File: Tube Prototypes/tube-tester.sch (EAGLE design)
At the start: 33 parts, among them IC1 NE555D, IC2 74141N, IC3 7805, Q1 IRF740S, Q2 BC546

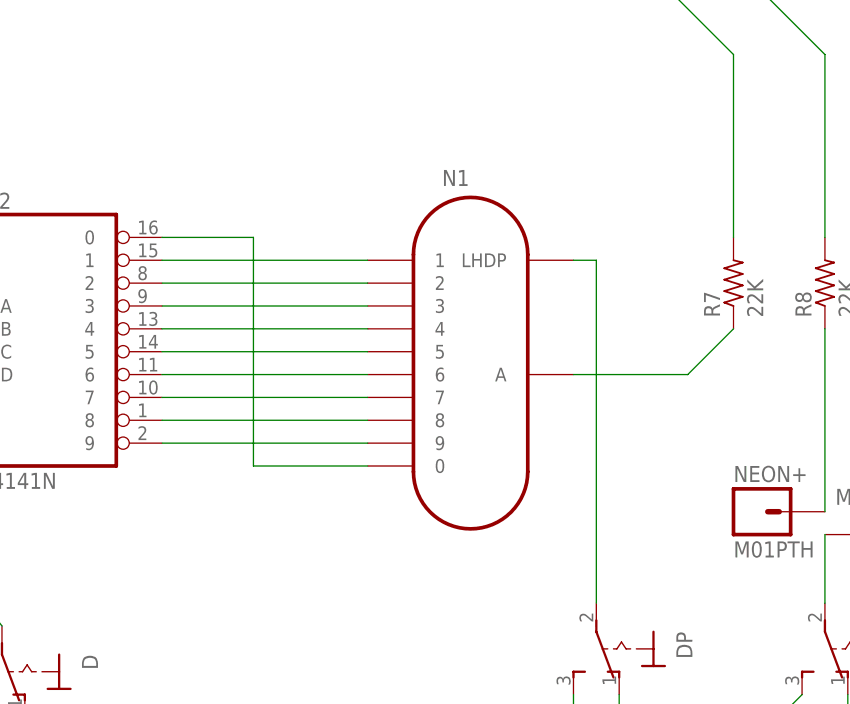
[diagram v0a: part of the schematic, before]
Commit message: new 180V and tube tester
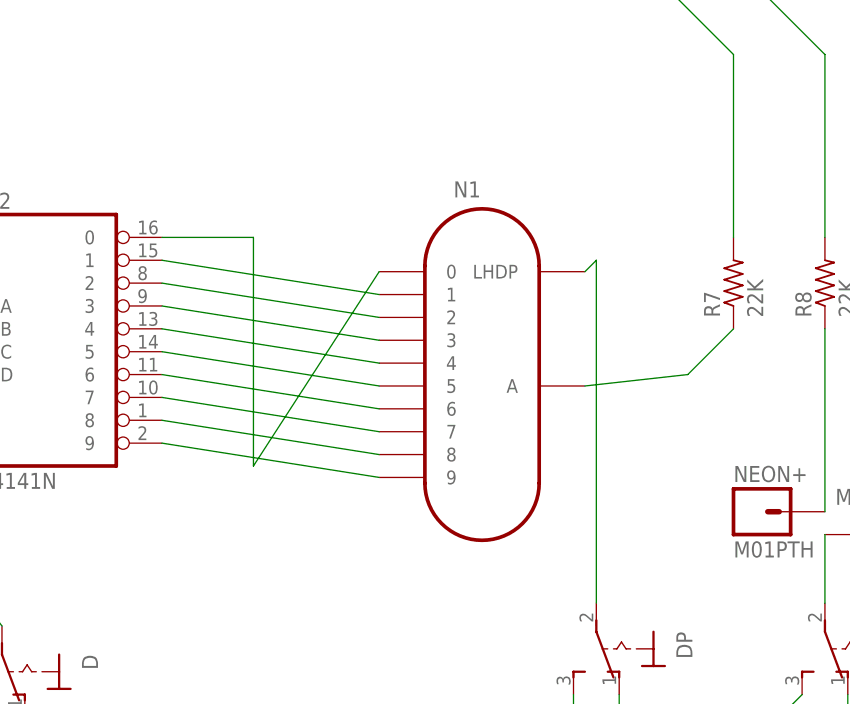
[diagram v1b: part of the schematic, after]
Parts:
- N1: value IN-12BIN-12 -> IN-12B; device iStivi - Tubes:IN-12BIN-12 -> iStivi - Tubes:IN-12B
- Q2: device iStivi - Transistor-FET:BC546B -> iStivi - Transistor-FET-reg:BC546A
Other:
- moved on the sheet: N1
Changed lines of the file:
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@@
 <part name="R6" library="iStivi - RCLD" deviceset="RESISTOR" device="R1206" value="2K2"/>
 <part name="C3" library="iStivi - RCLD" deviceset="CAPACITOR" device="C1206K" value="100pF"/>
-<part name="Q2" library="iStivi - Transistor-FET" deviceset="BC546*" device="" technology="B" value="BC546"/>
+<part name="Q2" library="iStivi - Transistor-FET-reg" deviceset="BC546*" device="" technology="A" value="BC546"/>
 <part name="C2" library="iStivi - RCLD" deviceset="CAPACITOR" device="C1206K" value="2n2"/>
 <part name="L1" library="iStivi - RCLD" deviceset="INDUCTOR" device="0207/10" value="100uH"/>
@@
 <part name="GND1" library="iStivi - Supply" deviceset="GND" device=""/>
 <part name="IC2" library="iStivi - ICs" deviceset="74*141" device="N"/>
-<part name="N1" library="iStivi - Tubes" deviceset="IN-12B" device="IN-12"/>
+<part name="N1" library="iStivi - Tubes" deviceset="IN-12B" device=""/>
 <part name="R7" library="iStivi - RCLD" deviceset="RESISTOR" device="0207/10" value="22K"/>
 <part name="A" library="iStivi - Button-Switch" deviceset="320-916" device=""/>
@@
 <pinref part="N1" gate="G$1" pin="1"/>
 <pinref part="IC2" gate="A" pin="1"/>
-<wire x1="213.36" y1="73.66" x2="190.5" y2="73.66" width="0.1524" layer="91"/>
+<wire x1="214.63" y1="69.85" x2="190.5" y2="73.66" width="0.1524" layer="91"/>
 </segment>
 </net>
@@
 <pinref part="N1" gate="G$1" pin="2"/>
 <pinref part="IC2" gate="A" pin="2"/>
-<wire x1="213.36" y1="71.12" x2="190.5" y2="71.12" width="0.1524" layer="91"/>
+<wire x1="214.63" y1="67.31" x2="190.5" y2="71.12" width="0.1524" layer="91"/>
 </segment>
 </net>
@@
 <pinref part="N1" gate="G$1" pin="3"/>
 <pinref part="IC2" gate="A" pin="3"/>
-<wire x1="213.36" y1="68.58" x2="190.5" y2="68.58" width="0.1524" layer="91"/>
+<wire x1="214.63" y1="64.77" x2="190.5" y2="68.58" width="0.1524" layer="91"/>
 </segment>
 </net>
@@
 <pinref part="N1" gate="G$1" pin="4"/>
 <pinref part="IC2" gate="A" pin="4"/>
-<wire x1="213.36" y1="66.04" x2="190.5" y2="66.04" width="0.1524" layer="91"/>
+<wire x1="214.63" y1="62.23" x2="190.5" y2="66.04" width="0.1524" layer="91"/>
 </segment>
 </net>
@@
 <pinref part="N1" gate="G$1" pin="5"/>
 <pinref part="IC2" gate="A" pin="5"/>
-<wire x1="213.36" y1="63.5" x2="190.5" y2="63.5" width="0.1524" layer="91"/>
+<wire x1="214.63" y1="59.69" x2="190.5" y2="63.5" width="0.1524" layer="91"/>
 </segment>
 </net>
@@
 <pinref part="N1" gate="G$1" pin="6"/>
 <pinref part="IC2" gate="A" pin="6"/>
-<wire x1="213.36" y1="60.96" x2="190.5" y2="60.96" width="0.1524" layer="91"/>
+<wire x1="214.63" y1="57.15" x2="190.5" y2="60.96" width="0.1524" layer="91"/>
 </segment>
 </net>
@@
 <pinref part="N1" gate="G$1" pin="7"/>
 <pinref part="IC2" gate="A" pin="7"/>
-<wire x1="213.36" y1="58.42" x2="190.5" y2="58.42" width="0.1524" layer="91"/>
+<wire x1="214.63" y1="54.61" x2="190.5" y2="58.42" width="0.1524" layer="91"/>
 </segment>
 </net>
@@
 <pinref part="N1" gate="G$1" pin="8"/>
 <pinref part="IC2" gate="A" pin="8"/>
-<wire x1="213.36" y1="55.88" x2="190.5" y2="55.88" width="0.1524" layer="91"/>
+<wire x1="214.63" y1="52.07" x2="190.5" y2="55.88" width="0.1524" layer="91"/>
 </segment>
 </net>
@@
 <pinref part="N1" gate="G$1" pin="9"/>
 <pinref part="IC2" gate="A" pin="9"/>
-<wire x1="213.36" y1="53.34" x2="190.5" y2="53.34" width="0.1524" layer="91"/>
+<wire x1="214.63" y1="49.53" x2="190.5" y2="53.34" width="0.1524" layer="91"/>
 </segment>
 </net>
@@
 <segment>
 <pinref part="N1" gate="G$1" pin="0"/>
-<wire x1="213.36" y1="50.8" x2="200.66" y2="50.8" width="0.1524" layer="91"/>
+<wire x1="214.63" y1="72.39" x2="200.66" y2="50.8" width="0.1524" layer="91"/>
 <wire x1="200.66" y1="50.8" x2="200.66" y2="76.2" width="0.1524" layer="91"/>
 <pinref part="IC2" gate="A" pin="0"/>
@@
 <pinref part="N1" gate="G$1" pin="A"/>
 <wire x1="254" y1="66.04" x2="248.92" y2="60.96" width="0.1524" layer="91"/>
-<wire x1="248.92" y1="60.96" x2="236.22" y2="60.96" width="0.1524" layer="91"/>
+<wire x1="248.92" y1="60.96" x2="237.49" y2="59.69" width="0.1524" layer="91"/>
 </segment>
 </net>
@@
 <pinref part="N1" gate="G$1" pin="LHDP"/>
 <pinref part="DP" gate="1" pin="P"/>
-<wire x1="236.22" y1="73.66" x2="238.76" y2="73.66" width="0.1524" layer="91"/>
+<wire x1="237.49" y1="72.39" x2="238.76" y2="73.66" width="0.1524" layer="91"/>
 <wire x1="238.76" y1="73.66" x2="238.76" y2="35.56" width="0.1524" layer="91"/>
 </segment>

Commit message: tube tester redo
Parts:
- removed C5: 100uF, iStivi - RCLD:CAPACITOR_POLE2-5
- IC3: device iStivi - Transistor-FET-reg:7805TV -> iStivi - Transistor-FET-reg:7805T
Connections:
- net GND: no longer C5.-
- net N$26: no longer C5.+
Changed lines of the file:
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@@
 <setting verticaltext="up"/>
 </settings>
-<grid distance="0.1" unitdist="inch" unit="inch" style="lines" multiple="1" display="no" altdistance="0.01" altunitdist="inch" altunit="inch"/>
+<grid distance="0.05" unitdist="inch" unit="inch" style="lines" multiple="1" display="yes" altdistance="0.025" altunitdist="inch" altunit="inch"/>
 <layers>
-<layer number="1" name="Top" color="4" fill="1" visible="no" active="no"/>
-<layer number="2" name="Route2" color="1" fill="3" visible="no" active="no"/>
-<layer number="3" name="Route3" color="4" fill="3" visible="no" active="no"/>
-<layer number="14" name="Route14" color="1" fill="6" visible="no" active="no"/>
-<layer number="15" name="Route15" color="4" fill="6" visible="no" active="no"/>
-<layer number="16" name="Bottom" color="1" fill="1" visible="no" active="no"/>
-<layer number="17" name="Pads" color="2" fill="1" visible="no" active="no"/>
-<layer number="18" name="Vias" color="2" fill="1" visible="no" active="no"/>
-<layer number="19" name="Unrouted" color="6" fill="1" visible="no" active="no"/>
-<layer number="20" name="Dimension" color="15" fill="1" visible="no" active="no"/>
-<layer number="21" name="tPlace" color="7" fill="1" visible="no" active="no"/>
-<layer number="22" name="bPlace" color="7" fill="1" visible="no" active="no"/>
-<layer number="23" name="tOrigins" color="15" fill="1" visible="no" active="no"/>
-<layer number="24" name="bOrigins" color="15" fill="1" visible="no" active="no"/>
-<layer number="25" name="tNames" color="7" fill="1" visible="no" active="no"/>
-<layer number="26" name="bNames" color="7" fill="1" visible="no" active="no"/>
-<layer number="27" name="tValues" color="7" fill="1" visible="no" active="no"/>
-<layer number="28" name="bValues" color="7" fill="1" visible="no" active="no"/>
+<layer number="1" name="Top" color="4" fill="1" visible="yes" active="no"/>
+<layer number="2" name="Route2" color="1" fill="3" visible="yes" active="no"/>
+<layer number="3" name="Route3" color="4" fill="3" visible="yes" active="no"/>
+<layer number="14" name="Route14" color="1" fill="6" visible="yes" active="no"/>
+<layer number="15" name="Route15" color="4" fill="6" visible="yes" active="no"/>
+<layer number="16" name="Bottom" color="1" fill="1" visible="yes" active="no"/>
+<layer number="17" name="Pads" color="2" fill="1" visible="yes" active="no"/>
+<layer number="18" name="Vias" color="2" fill="1" visible="yes" active="no"/>
+<layer number="19" name="Unrouted" color="6" fill="1" visible="yes" active="no"/>
+<layer number="20" name="Dimension" color="15" fill="1" visible="yes" active="no"/>
+<layer number="21" name="tPlace" color="7" fill="1" visible="yes" active="no"/>
+<layer number="22" name="bPlace" color="7" fill="1" visible="yes" active="no"/>
+<layer number="23" name="tOrigins" color="15" fill="1" visible="yes" active="no"/>
+<layer number="24" name="bOrigins" color="15" fill="1" visible="yes" active="no"/>
+<layer number="25" name="tNames" color="7" fill="1" visible="yes" active="no"/>
+<layer number="26" name="bNames" color="7" fill="1" visible="yes" active="no"/>
+<layer number="27" name="tValues" color="7" fill="1" visible="yes" active="no"/>
+<layer number="28" name="bValues" color="7" fill="1" visible="yes" active="no"/>
 <layer number="29" name="tStop" color="7" fill="3" visible="no" active="no"/>
 <layer number="30" name="bStop" color="7" fill="6" visible="no" active="no"/>
@@
 <layer number="35" name="tGlue" color="7" fill="4" visible="no" active="no"/>
 <layer number="36" name="bGlue" color="7" fill="5" visible="no" active="no"/>
-<layer number="37" name="tTest" color="7" fill="1" visible="no" active="no"/>
-<layer number="38" name="bTest" color="7" fill="1" visible="no" active="no"/>
+<layer number="37" name="tTest" color="7" fill="1" visible="yes" active="no"/>
+<layer number="38" name="bTest" color="7" fill="1" visible="yes" active="no"/>
 <layer number="39" name="tKeepout" color="4" fill="11" visible="no" active="no"/>
 <layer number="40" name="bKeepout" color="1" fill="11" visible="no" active="no"/>
@@
 <layer number="44" name="Drills" color="7" fill="1" visible="no" active="no"/>
 <layer number="45" name="Holes" color="7" fill="1" visible="no" active="no"/>
-<layer number="46" name="Milling" color="3" fill="1" visible="no" active="no"/>
-<layer number="47" name="Measures" color="7" fill="1" visible="no" active="no"/>
-<layer number="48" name="Document" color="7" fill="1" visible="no" active="no"/>
-<layer number="49" name="Reference" color="7" fill="1" visible="no" active="no"/>
-<layer number="50" name="dxf" color="7" fill="1" visible="no" active="no"/>
-<layer number="51" name="tDocu" color="7" fill="1" visible="no" active="no"/>
-<layer number="52" name="bDocu" color="7" fill="1" visible="no" active="no"/>
-<layer number="53" name="tGND_GNDA" color="7" fill="9" visible="no" active="no"/>
-<layer number="54" name="bGND_GNDA" color="1" fill="9" visible="no" active="no"/>
-<layer number="56" name="wert" color="7" fill="1" visible="no" active="no"/>
+<layer number="46" name="Milling" color="3" fill="1" visible="yes" active="no"/>
+<layer number="47" name="Measures" color="7" fill="1" visible="yes" active="no"/>
+<layer number="48" name="Document" color="7" fill="1" visible="yes" active="no"/>
+<layer number="49" name="Reference" color="7" fill="1" visible="yes" active="no"/>
+<layer number="50" name="dxf" color="7" fill="1" visible="yes" active="no"/>
+<layer number="51" name="tDocu" color="7" fill="1" visible="yes" active="no"/>
+<layer number="52" name="bDocu" color="7" fill="1" visible="yes" active="no"/>
+<layer number="53" name="tGND_GNDA" color="7" fill="9" visible="yes" active="no"/>
+<layer number="54" name="bGND_GNDA" color="1" fill="9" visible="yes" active="no"/>
+<layer number="56" name="wert" color="7" fill="1" visible="yes" active="no"/>
 <layer number="91" name="Nets" color="2" fill="1" visible="yes" active="yes"/>
 <layer number="92" name="Busses" color="1" fill="1" visible="yes" active="yes"/>
@@
 <part name="C" library="iStivi - Button-Switch" deviceset="320-916" device=""/>
 <part name="D" library="iStivi - Button-Switch" deviceset="320-916" device=""/>
-<part name="IC3" library="iStivi - Transistor-FET-reg" deviceset="78*" device="TV" technology="05" value="7805"/>
+<part name="IC3" library="iStivi - Transistor-FET-reg" deviceset="78*" device="T" technology="05" value="7805"/>
 <part name="JP1" library="iStivi - Header-Connector" deviceset="M02" device="3.5MM"/>
-<part name="C5" library="iStivi - RCLD" deviceset="CAPACITOR_POL" device="E2-5" value="100uF"/>
 <part name="C6" library="iStivi - RCLD" deviceset="CAPACITOR_POL" device="E2-5" value="10uF"/>
 <part name="R8" library="iStivi - RCLD" deviceset="RESISTOR" device="0207/10" value="22K"/>
@@
 <instance part="IC3" gate="A1" x="124.46" y="106.68"/>
 <instance part="JP1" gate="G$1" x="81.28" y="114.3" rot="MR270"/>
-<instance part="C5" gate="G$1" x="104.14" y="99.06"/>
 <instance part="C6" gate="G$1" x="142.24" y="99.06"/>
 <instance part="IC2" gate="P" x="152.4" y="96.52"/>
@@
 <wire x1="152.4" y1="83.82" x2="142.24" y2="83.82" width="0.1524" layer="91"/>
 <junction x="124.46" y="83.82"/>
-<pinref part="C5" gate="G$1" pin="-"/>
 <wire x1="142.24" y1="83.82" x2="124.46" y2="83.82" width="0.1524" layer="91"/>
-<wire x1="104.14" y1="93.98" x2="104.14" y2="83.82" width="0.1524" layer="91"/>
-<wire x1="104.14" y1="83.82" x2="124.46" y2="83.82" width="0.1524" layer="91"/>
 <pinref part="C6" gate="G$1" pin="-"/>
 <wire x1="142.24" y1="93.98" x2="142.24" y2="83.82" width="0.1524" layer="91"/>
@@
 <pinref part="JP1" gate="G$1" pin="1"/>
 <wire x1="81.28" y1="81.28" x2="81.28" y2="106.68" width="0.1524" layer="91"/>
-<pinref part="C5" gate="G$1" pin="+"/>
 <pinref part="IC3" gate="A1" pin="VI"/>
-<wire x1="104.14" y1="101.6" x2="104.14" y2="106.68" width="0.1524" layer="91"/>
-<wire x1="104.14" y1="106.68" x2="114.3" y2="106.68" width="0.1524" layer="91"/>
-<wire x1="81.28" y1="106.68" x2="104.14" y2="106.68" width="0.1524" layer="91"/>
+<wire x1="81.28" y1="106.68" x2="114.3" y2="106.68" width="0.1524" layer="91"/>
 <junction x="81.28" y="106.68"/>
-<junction x="104.14" y="106.68"/>
-</segment>
-</net>
+</segment>
+</net>
